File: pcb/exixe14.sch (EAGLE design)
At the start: 51 parts

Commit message: updated to use timer
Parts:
- R1, R10, R11, R12, R17, R18, R2, R24, R3, R4, R5, R7, R8, R9: value 4K7 -> 10K
- R20, R21: value 4K7 -> 510K
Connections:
- removed net UART_RX: TP4.TP, U$2.PB7
- new net N$25: TP4.TP, U$2.PB3
- net STM_4: now also U$2.PB7; no longer U$2.PB5
- net STM_7: now also U$2.PB5; no longer U$2.PB4
- net STM_DOT_LEFT: now also U$2.PB4; no longer U$2.PB3
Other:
- moved on the sheet: TP4
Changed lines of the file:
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@@
 <part name="P+2" library="nixx" deviceset="+180V" device=""/>
 <part name="P+1" library="nixx" deviceset="+180V" device=""/>
-<part name="R1" library="joyAnalog" deviceset="RESISTOR" device="0805-RES" value="4K7"/>
+<part name="R1" library="joyAnalog" deviceset="RESISTOR" device="0805-RES" value="10K"/>
 <part name="C1" library="joyAnalog" deviceset="CAP" device="0805" value="1uF"/>
 <part name="GND1" library="joyAnalog" deviceset="GND" device=""/>
 <part name="Q2" library="nixx" deviceset="BF820" device=""/>
-<part name="R2" library="joyAnalog" deviceset="RESISTOR" device="0805-RES" value="4K7"/>
+<part name="R2" library="joyAnalog" deviceset="RESISTOR" device="0805-RES" value="10K"/>
 <part name="GND2" library="joyAnalog" deviceset="GND" device=""/>
 <part name="Q3" library="nixx" deviceset="BF820" device=""/>
-<part name="R3" library="joyAnalog" deviceset="RESISTOR" device="0805-RES" value="4K7"/>
+<part name="R3" library="joyAnalog" deviceset="RESISTOR" device="0805-RES" value="10K"/>
 <part name="GND3" library="joyAnalog" deviceset="GND" device=""/>
 <part name="Q4" library="nixx" deviceset="BF820" device=""/>
-<part name="R4" library="joyAnalog" deviceset="RESISTOR" device="0805-RES" value="4K7"/>
+<part name="R4" library="joyAnalog" deviceset="RESISTOR" device="0805-RES" value="10K"/>
 <part name="GND4" library="joyAnalog" deviceset="GND" device=""/>
 <part name="Q5" library="nixx" deviceset="BF820" device=""/>
-<part name="R5" library="joyAnalog" deviceset="RESISTOR" device="0805-RES" value="4K7"/>
+<part name="R5" library="joyAnalog" deviceset="RESISTOR" device="0805-RES" value="10K"/>
 <part name="GND5" library="joyAnalog" deviceset="GND" device=""/>
 <part name="Q6" library="nixx" deviceset="BF820" device=""/>
@@
 <part name="GND6" library="joyAnalog" deviceset="GND" device=""/>
 <part name="Q7" library="nixx" deviceset="BF820" device=""/>
-<part name="R7" library="joyAnalog" deviceset="RESISTOR" device="0805-RES" value="4K7"/>
+<part name="R7" library="joyAnalog" deviceset="RESISTOR" device="0805-RES" value="10K"/>
 <part name="GND7" library="joyAnalog" deviceset="GND" device=""/>
 <part name="Q8" library="nixx" deviceset="BF820" device=""/>
-<part name="R8" library="joyAnalog" deviceset="RESISTOR" device="0805-RES" value="4K7"/>
+<part name="R8" library="joyAnalog" deviceset="RESISTOR" device="0805-RES" value="10K"/>
 <part name="GND8" library="joyAnalog" deviceset="GND" device=""/>
 <part name="Q9" library="nixx" deviceset="BF820" device=""/>
-<part name="R9" library="joyAnalog" deviceset="RESISTOR" device="0805-RES" value="4K7"/>
+<part name="R9" library="joyAnalog" deviceset="RESISTOR" device="0805-RES" value="10K"/>
 <part name="GND9" library="joyAnalog" deviceset="GND" device=""/>
 <part name="Q10" library="nixx" deviceset="BF820" device=""/>
-<part name="R10" library="joyAnalog" deviceset="RESISTOR" device="0805-RES" value="4K7"/>
+<part name="R10" library="joyAnalog" deviceset="RESISTOR" device="0805-RES" value="10K"/>
 <part name="GND10" library="joyAnalog" deviceset="GND" device=""/>
 <part name="Q11" library="nixx" deviceset="BF820" device=""/>
-<part name="R11" library="joyAnalog" deviceset="RESISTOR" device="0805-RES" value="4K7"/>
+<part name="R11" library="joyAnalog" deviceset="RESISTOR" device="0805-RES" value="10K"/>
 <part name="GND11" library="joyAnalog" deviceset="GND" device=""/>
 <part name="Q12" library="nixx" deviceset="BF820" device=""/>
-<part name="R12" library="joyAnalog" deviceset="RESISTOR" device="0805-RES" value="4K7"/>
+<part name="R12" library="joyAnalog" deviceset="RESISTOR" device="0805-RES" value="10K"/>
 <part name="GND12" library="joyAnalog" deviceset="GND" device=""/>
 <part name="GND13" library="joyAnalog" deviceset="GND" device=""/>
@@
 <part name="R15" library="joyAnalog" deviceset="RESISTOR" device="0805-RES" value="1K"/>
 <part name="R16" library="joyAnalog" deviceset="RESISTOR" device="0805-RES" value="470"/>
-<part name="R17" library="joyAnalog" deviceset="RESISTOR" device="0805-RES" value="4K7"/>
-<part name="R18" library="joyAnalog" deviceset="RESISTOR" device="0805-RES" value="4K7"/>
+<part name="R17" library="joyAnalog" deviceset="RESISTOR" device="0805-RES" value="10K"/>
+<part name="R18" library="joyAnalog" deviceset="RESISTOR" device="0805-RES" value="10K"/>
 <part name="+3V5" library="joyAnalog" deviceset="+3V3" device=""/>
 <part name="+3V6" library="joyAnalog" deviceset="+3V3" device=""/>
@@
 <part name="T1" library="zetex" deviceset="PNPSOT323" device=""/>
 <part name="Q13" library="nixx" deviceset="BF820" device=""/>
-<part name="R24" library="joyAnalog" deviceset="RESISTOR" device="0805-RES" value="4K7"/>
+<part name="R24" library="joyAnalog" deviceset="RESISTOR" device="0805-RES" value="10K"/>
 <part name="GND18" library="joyAnalog" deviceset="GND" device=""/>
 <part name="R19" library="joyAnalog" deviceset="RESISTOR" device="0805-RES" value="1M"/>
 <part name="TP2" library="testpad" deviceset="PTR1" device="TP13R" value="PTR1TP13R"/>
 <part name="TP3" library="testpad" deviceset="PTR1" device="TP13R" value="PTR1TP13R"/>
-<part name="TP4" library="testpad" deviceset="PTR1" device="TP13R" value="PTR1TP13R"/>
-<part name="R20" library="joyAnalog" deviceset="RESISTOR" device="0805-RES" value="4K7"/>
-<part name="R21" library="joyAnalog" deviceset="RESISTOR" device="0805-RES" value="4K7"/>
+<part name="R20" library="joyAnalog" deviceset="RESISTOR" device="0805-RES" value="510K"/>
+<part name="R21" library="joyAnalog" deviceset="RESISTOR" device="0805-RES" value="510K"/>
 <part name="R25" library="joyAnalog" deviceset="RESISTOR" device="0805-RES" value="68K"/>
 <part name="GND16" library="joyAnalog" deviceset="GND" device=""/>
+<part name="TP4" library="testpad" deviceset="PTR1" device="TP13R" value="PTR1TP13R"/>
 </parts>
 <sheets>
@@
 <instance part="TP2" gate="G$1" x="381" y="53.34" rot="R270"/>
 <instance part="TP3" gate="G$1" x="441.96" y="43.18" rot="R90"/>
-<instance part="TP4" gate="G$1" x="441.96" y="40.64" rot="R90"/>
 <instance part="R20" gate="G$1" x="238.76" y="53.34"/>
 <instance part="R21" gate="G$1" x="238.76" y="27.94"/>
 <instance part="R25" gate="G$1" x="429.26" y="33.02" rot="R90"/>
 <instance part="GND16" gate="1" x="429.26" y="25.4"/>
+<instance part="TP4" gate="G$1" x="452.12" y="50.8" rot="R90"/>
 </instances>
 <busses>
@@
 </segment>
 </net>
-<net name="UART_RX" class="0">
-<segment>
-<pinref part="U$2" gate="G$1" pin="PB7"/>
-<wire x1="439.42" y1="40.64" x2="424.18" y2="40.64" width="0.1524" layer="91"/>
-<label x="426.72" y="40.64" size="1.778" layer="95"/>
-<pinref part="TP4" gate="G$1" pin="TP"/>
-</segment>
-</net>
 <net name="UART_TX" class="0">
 <segment>
@@
 </segment>
 <segment>
-<label x="426.72" y="50.8" size="1.778" layer="95"/>
-<pinref part="U$2" gate="G$1" pin="PB3"/>
-<wire x1="439.42" y1="50.8" x2="424.18" y2="50.8" width="0.1524" layer="91"/>
+<label x="426.72" y="48.26" size="1.778" layer="95"/>
+<pinref part="U$2" gate="G$1" pin="PB4"/>
+<wire x1="439.42" y1="48.26" x2="424.18" y2="48.26" width="0.1524" layer="91"/>
 </segment>
 </net>
@@
 </segment>
 <segment>
-<pinref part="U$2" gate="G$1" pin="PB4"/>
-<wire x1="439.42" y1="48.26" x2="424.18" y2="48.26" width="0.1524" layer="91"/>
-<label x="426.72" y="48.26" size="1.778" layer="95"/>
+<label x="426.72" y="45.72" size="1.778" layer="95"/>
+<pinref part="U$2" gate="G$1" pin="PB5"/>
+<wire x1="439.42" y1="45.72" x2="424.18" y2="45.72" width="0.1524" layer="91"/>
 </segment>
 </net>
@@
 </segment>
 <segment>
-<pinref part="U$2" gate="G$1" pin="PB5"/>
-<wire x1="439.42" y1="45.72" x2="424.18" y2="45.72" width="0.1524" layer="91"/>
-<label x="426.72" y="45.72" size="1.778" layer="95"/>
+<label x="426.72" y="40.64" size="1.778" layer="95"/>
+<pinref part="U$2" gate="G$1" pin="PB7"/>
+<wire x1="439.42" y1="40.64" x2="424.18" y2="40.64" width="0.1524" layer="91"/>
 </segment>
 </net>
@@
 </segment>
 </net>
+<net name="N$25" class="0">
+<segment>
+<pinref part="U$2" gate="G$1" pin="PB3"/>
+<pinref part="TP4" gate="G$1" pin="TP"/>
+<wire x1="424.18" y1="50.8" x2="449.58" y2="50.8" width="0.1524" layer="91"/>
+</segment>
+</net>

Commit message: adjusted values
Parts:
- R14, R16: value 470 -> 330
- R15: value 1K -> 680
- R23: value 100K -> 68K
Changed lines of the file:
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@@
 <part name="R13" library="joyAnalog" deviceset="RESISTOR" device="0805-RES" value="68K"/>
 <part name="+3V4" library="joyAnalog" deviceset="+3V3" device=""/>
-<part name="R14" library="joyAnalog" deviceset="RESISTOR" device="0805-RES" value="470"/>
-<part name="R15" library="joyAnalog" deviceset="RESISTOR" device="0805-RES" value="1K"/>
-<part name="R16" library="joyAnalog" deviceset="RESISTOR" device="0805-RES" value="470"/>
+<part name="R14" library="joyAnalog" deviceset="RESISTOR" device="0805-RES" value="330"/>
+<part name="R15" library="joyAnalog" deviceset="RESISTOR" device="0805-RES" value="680"/>
+<part name="R16" library="joyAnalog" deviceset="RESISTOR" device="0805-RES" value="330"/>
 <part name="R17" library="joyAnalog" deviceset="RESISTOR" device="0805-RES" value="10K"/>
 <part name="R18" library="joyAnalog" deviceset="RESISTOR" device="0805-RES" value="10K"/>
@@
 <part name="TP1" library="testpad" deviceset="PTR1" device="TP13R" value="PTR1TP13R"/>
 <part name="R22" library="joyAnalog" deviceset="RESISTOR" device="0805-RES" value="1M"/>
-<part name="R23" library="joyAnalog" deviceset="RESISTOR" device="0805-RES" value="100K"/>
+<part name="R23" library="joyAnalog" deviceset="RESISTOR" device="0805-RES" value="68K"/>
 <part name="T1" library="zetex" deviceset="PNPSOT323" device=""/>
 <part name="Q13" library="nixx" deviceset="BF820" device=""/>

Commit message: more readme
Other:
- note added: "MSB92"
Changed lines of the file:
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@@
 <?xml version="1.0" encoding="utf-8"?>
 <!DOCTYPE eagle SYSTEM "eagle.dtd">
-<eagle version="8.2.2">
+<eagle version="8.3.2">
 <drawing>
 <settings>
 <setting alwaysvectorfont="no"/>
+<setting keepoldvectorfont="yes"/>
 <setting verticaltext="up"/>
 </settings>
@@
 <sheet>
 <plain>
+<text x="408.94" y="-66.04" size="1.778" layer="94">MSB92</text>
 </plain>
 <instances>

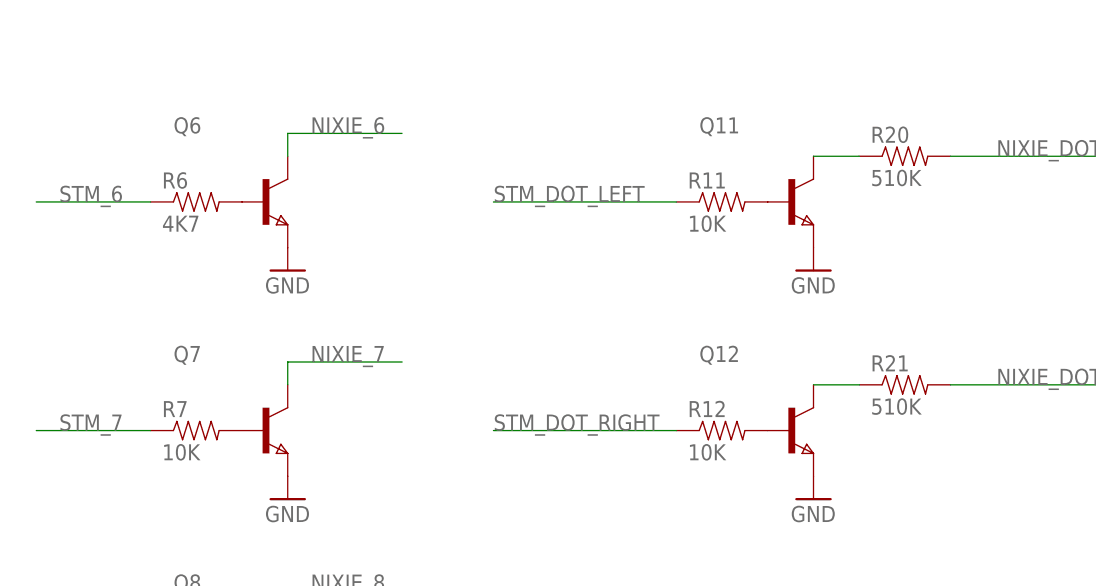
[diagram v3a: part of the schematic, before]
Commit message: adjust passive values and added bom
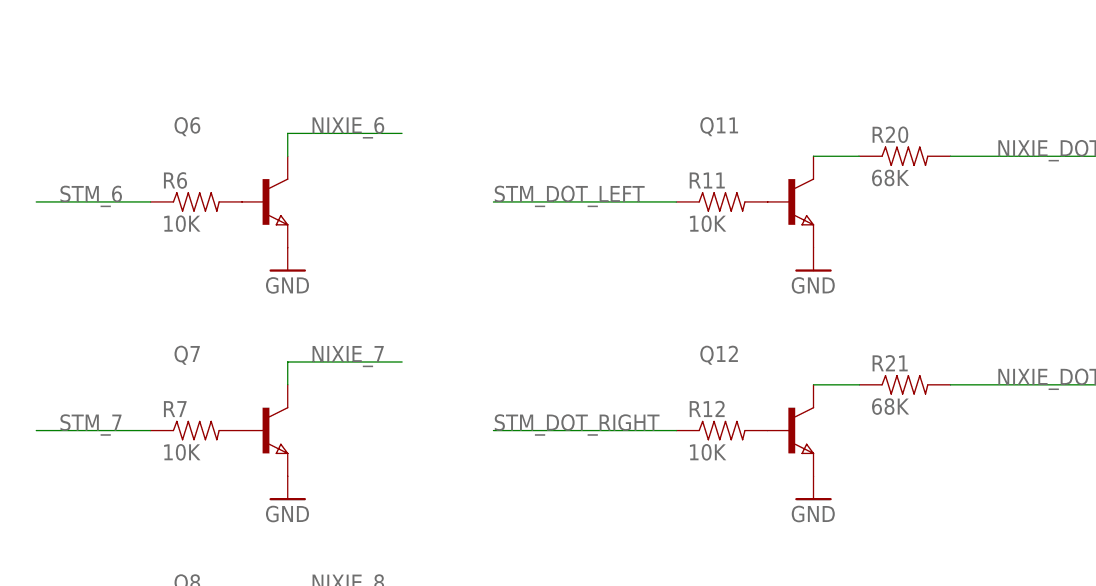
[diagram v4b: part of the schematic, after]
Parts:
- R20, R21: value 510K -> 68K
- R6: value 4K7 -> 10K
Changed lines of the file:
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@@
 <part name="GND5" library="joyAnalog" deviceset="GND" device=""/>
 <part name="Q6" library="nixx" deviceset="BF820" device=""/>
-<part name="R6" library="joyAnalog" deviceset="RESISTOR" device="0805-RES" value="4K7"/>
+<part name="R6" library="joyAnalog" deviceset="RESISTOR" device="0805-RES" value="10K"/>
 <part name="GND6" library="joyAnalog" deviceset="GND" device=""/>
 <part name="Q7" library="nixx" deviceset="BF820" device=""/>
@@
 <part name="TP2" library="testpad" deviceset="PTR1" device="TP13R" value="PTR1TP13R"/>
 <part name="TP3" library="testpad" deviceset="PTR1" device="TP13R" value="PTR1TP13R"/>
-<part name="R20" library="joyAnalog" deviceset="RESISTOR" device="0805-RES" value="510K"/>
-<part name="R21" library="joyAnalog" deviceset="RESISTOR" device="0805-RES" value="510K"/>
+<part name="R20" library="joyAnalog" deviceset="RESISTOR" device="0805-RES" value="68K"/>
+<part name="R21" library="joyAnalog" deviceset="RESISTOR" device="0805-RES" value="68K"/>
 <part name="R25" library="joyAnalog" deviceset="RESISTOR" device="0805-RES" value="68K"/>
 <part name="GND16" library="joyAnalog" deviceset="GND" device=""/>
